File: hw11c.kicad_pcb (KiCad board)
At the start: 2 copper layers, 49.5 x 27.5 mm, 64 parts, among them Q1 KX-7_12MHZ, SW1 BUTT1, SW2 BUTT2, X1 ~RESET, X10 PIO2.8, X11 PIO1.4, X12 ADC3, X13 PIO0.8, X14 PIO0.9, X15 MAT0, X2 SWCLK, X3 SWDIO, X4 SSEL1, X5 SCK1, X6 MISO1, X7 MOSI1, X8 PIO2.6, X9 PIO2.7

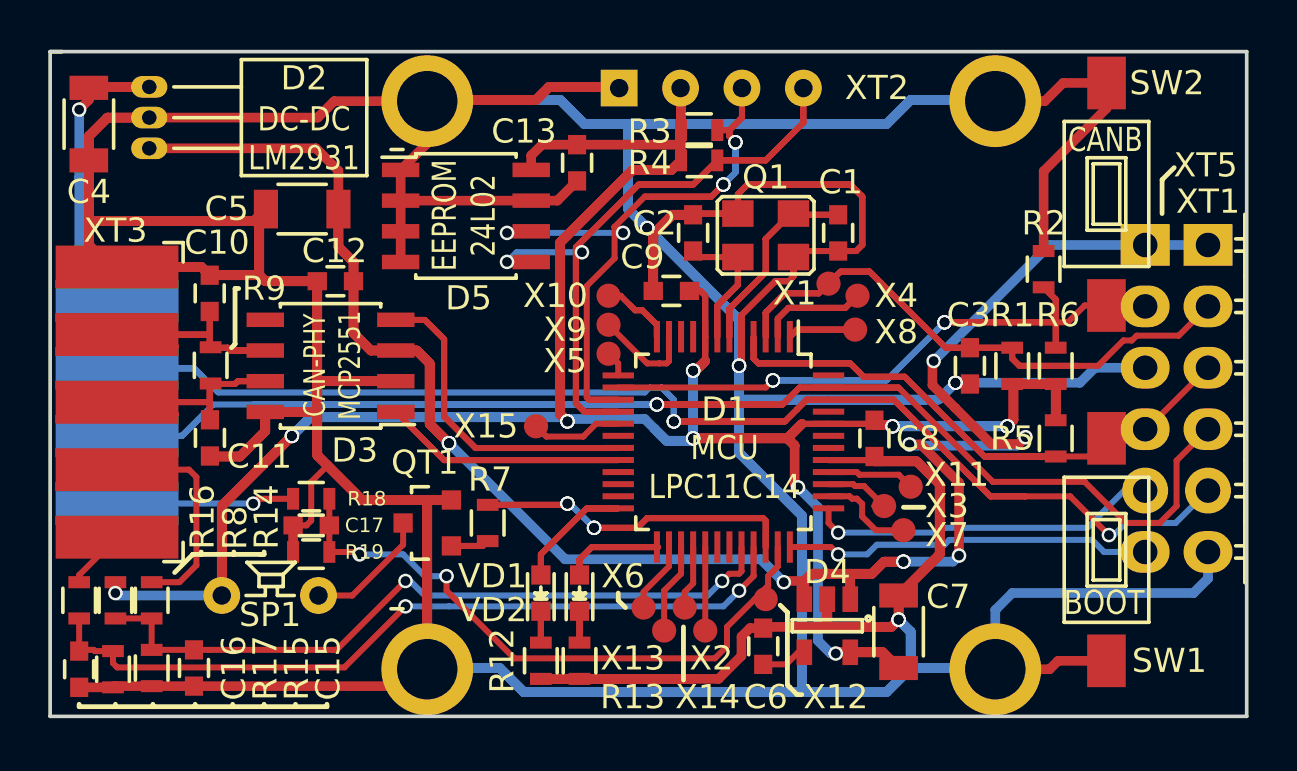
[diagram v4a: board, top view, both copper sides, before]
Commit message: Add R10, R11 to RX and TX lines.
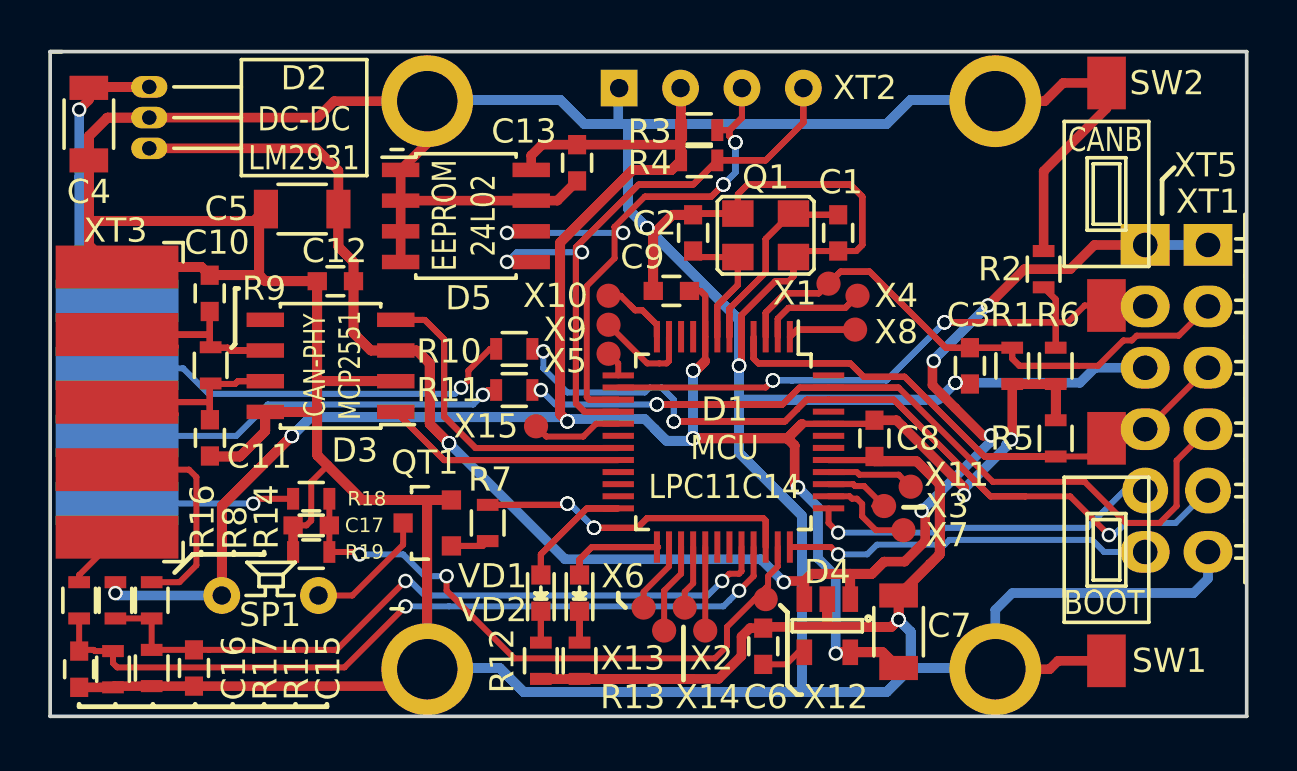
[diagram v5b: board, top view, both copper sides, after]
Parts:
- added R10: 0, libs:R_0603, F.Cu at (69.1, 62.3)
- added R11: 0, libs:R_0603, F.Cu at (69.1, 64.0)
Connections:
- XT3 pad 7: /RXD -> Net-(R10-Pad1)
- XT3 pad 8: /TXD -> Net-(R11-Pad1)
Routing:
- net /TXD: track 82.1 -> 43.9 mm, vias 2 -> 3
- net /RXD: track 72.1 -> 51.9 mm, vias 3 -> 4
- net Net-(R10-Pad1): track 0.00 -> 17.1 mm, vias 0 -> 1
- net Net-(R11-Pad1): track 0.00 -> 16.5 mm, vias 0 -> 1
- net GND: track 489.5 -> 474.7 mm
- net /5V: track 97.2 -> 88.5 mm, vias 9 -> 7
- net /3.3V: track 159.3 -> 155.1 mm, vias 15 -> 13

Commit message: Add X16/X17 pads. Fix buttons silk.
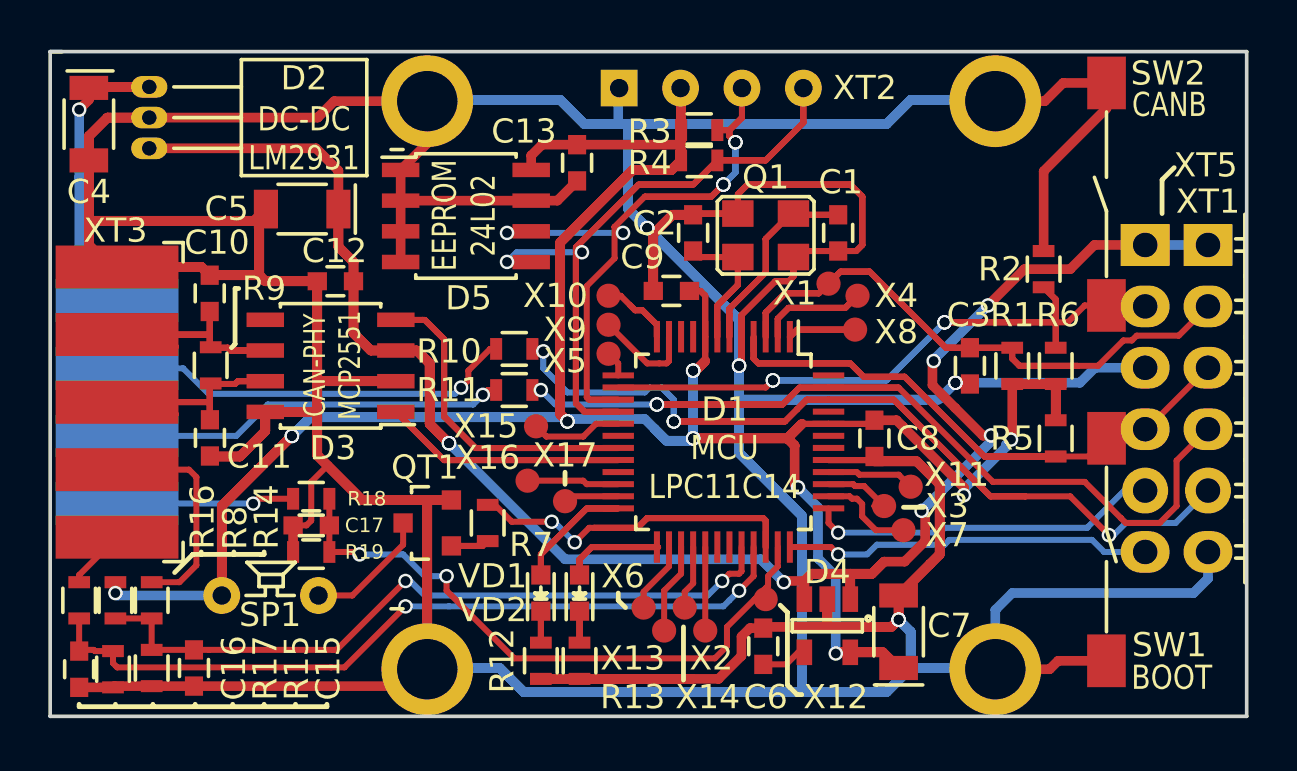
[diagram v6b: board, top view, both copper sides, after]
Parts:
- added X16: PIO0.6, libs:PAD, F.Cu at (69.7, 67.8)
- added X17: PIO0.7, libs:PAD, F.Cu at (71.2, 68.6)
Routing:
- net /BEEP: track 26.5 -> 22.1 mm, vias 4 -> 2
- net Net-(D1-Pad22): track 0.00 -> 3.81 mm
- net Net-(D1-Pad23): track 0.00 -> 2.29 mm

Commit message: Add holes at the edges of the board.
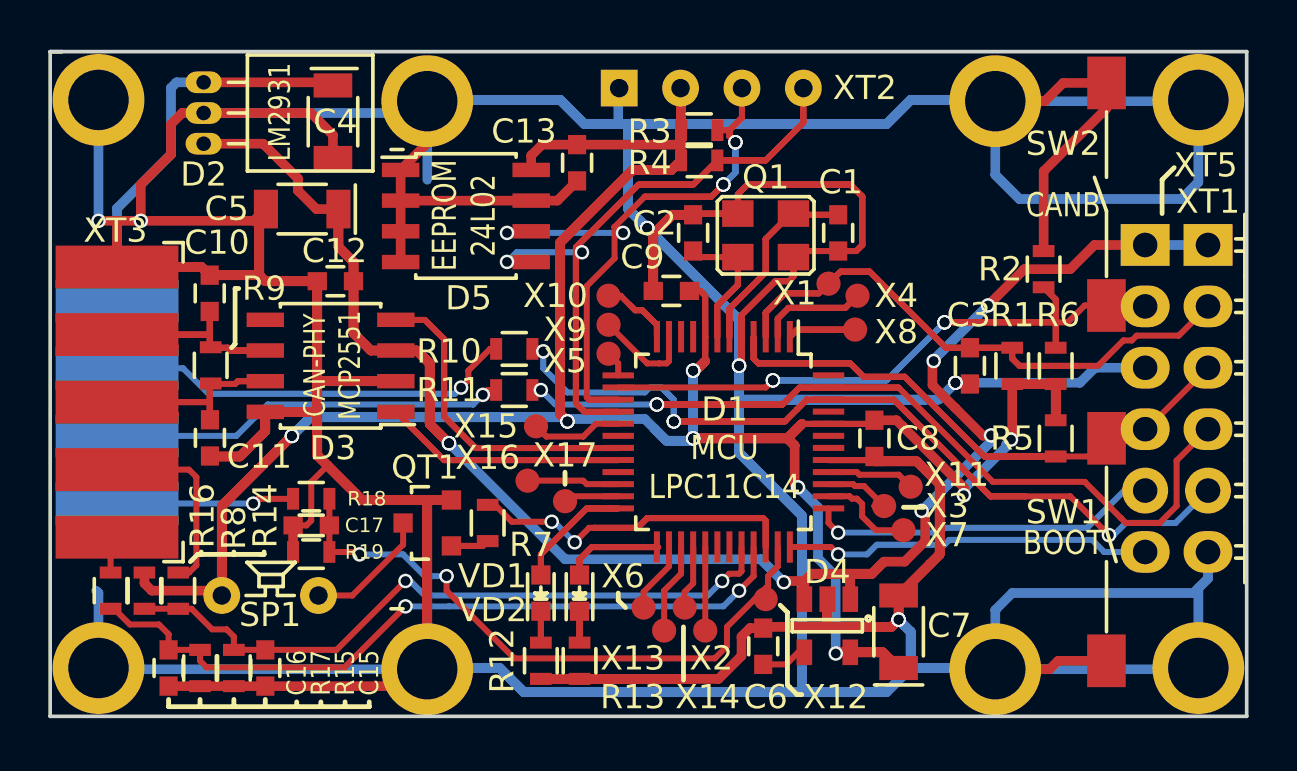
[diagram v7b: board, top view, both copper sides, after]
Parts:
- added REF**: Hole, libs:Hole, F.Cu at (97.4, 52.0)
- added REF**: Hole, libs:Hole, F.Cu at (97.4, 75.5)
- added REF**: Hole, libs:Hole, F.Cu at (51.9, 52.0)
- added REF**: Hole, libs:Hole, F.Cu at (51.9, 75.5)
- moved C4 10.1 mm to (61.6, 52.9)
- moved C16 3.70 mm to (54.8, 75.5)
- moved R17 3.60 mm to (56.1, 75.5)
- moved R15 3.40 mm to (57.5, 75.5)
- moved C15 2.95 mm to (58.8, 75.5)
- moved D2 2.26 mm to (56.2, 53.8)
- moved R16 1.36 mm to (52.4, 72.3)
- moved R8 1.26 mm to (53.8, 72.3)
- moved R14 1.17 mm to (55.2, 72.3)
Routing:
- net GND: track 474.7 -> 519.7 mm, vias 8 -> 10
- net /5V: track 88.5 -> 85.7 mm
- net /12V: track 14.9 -> 17.0 mm, vias 1 -> 0
- net /ADC1: track 32.6 -> 31.0 mm
- net /ADC0: track 30.0 -> 28.6 mm
- net /AN1: track 9.20 -> 7.93 mm
- net /3.3V: track 155.1 -> 154.1 mm, vias 13 -> 12
- net /AN2: track 2.51 -> 1.57 mm
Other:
- board text added: "LM2931"
- board text removed: "DC-DC LM2931"

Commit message: New board size: 49x27.5mm.
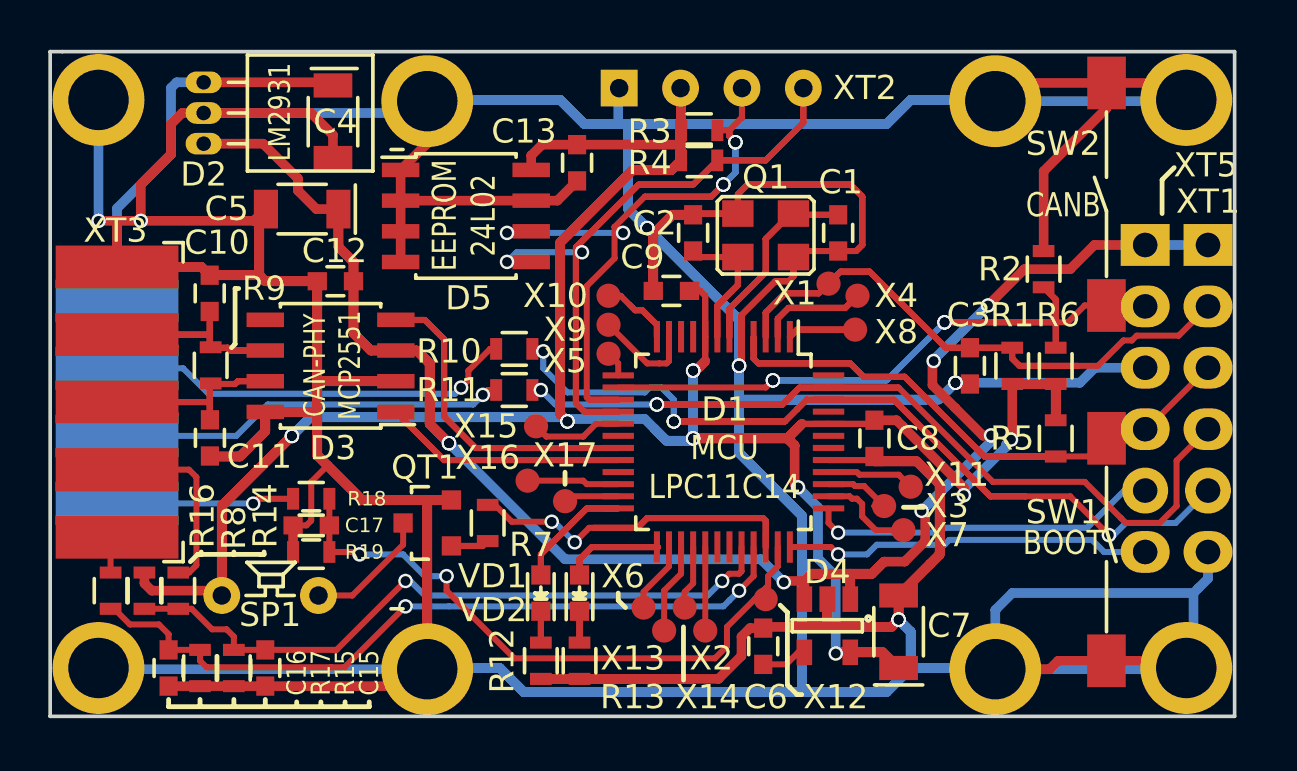
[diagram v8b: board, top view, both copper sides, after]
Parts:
- moved REF** 0.50 mm to (96.9, 52.0)
- moved REF** 0.50 mm to (96.9, 75.5)
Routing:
- net GND: track 519.7 -> 504.6 mm
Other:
- board size 49.5 x 27.5 mm -> 49 x 27.5 mm
